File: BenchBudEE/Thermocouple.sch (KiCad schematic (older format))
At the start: 0 parts

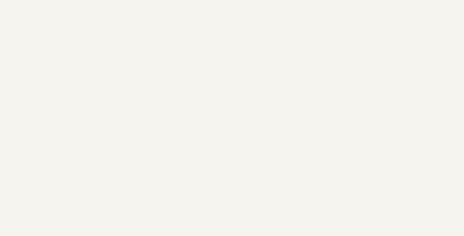
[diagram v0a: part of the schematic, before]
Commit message: Defined block inputs and outputs.
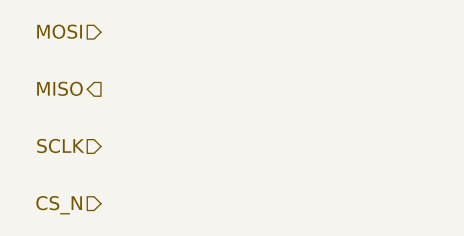
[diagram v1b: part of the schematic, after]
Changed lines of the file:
@@
 Text HLabel 5950 3150 2    60   Input ~ 0
 TC IN -
+Text HLabel 2300 2500 0    60   Input ~ 0
+MOSI
+Text HLabel 2300 2750 0    60   Output ~ 0
+MISO
+Text HLabel 2300 3000 0    60   Input ~ 0
+SCLK
+Text HLabel 2300 3250 0    60   Input ~ 0
+CS_N
 $EndSCHEMATC

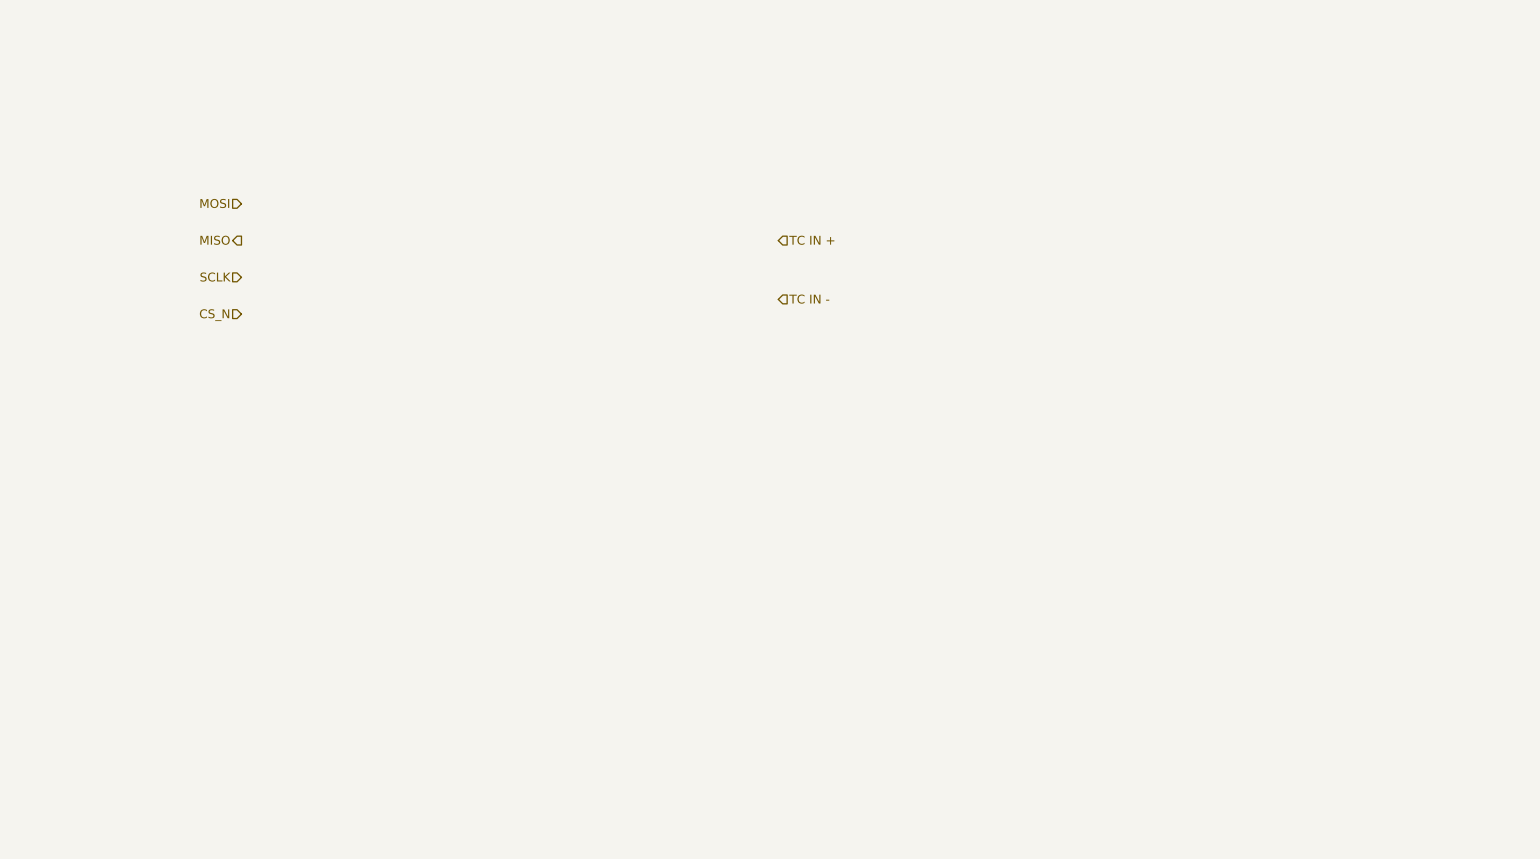
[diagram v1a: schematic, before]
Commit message: Fleshed out the thermocouple sheet, in block form.
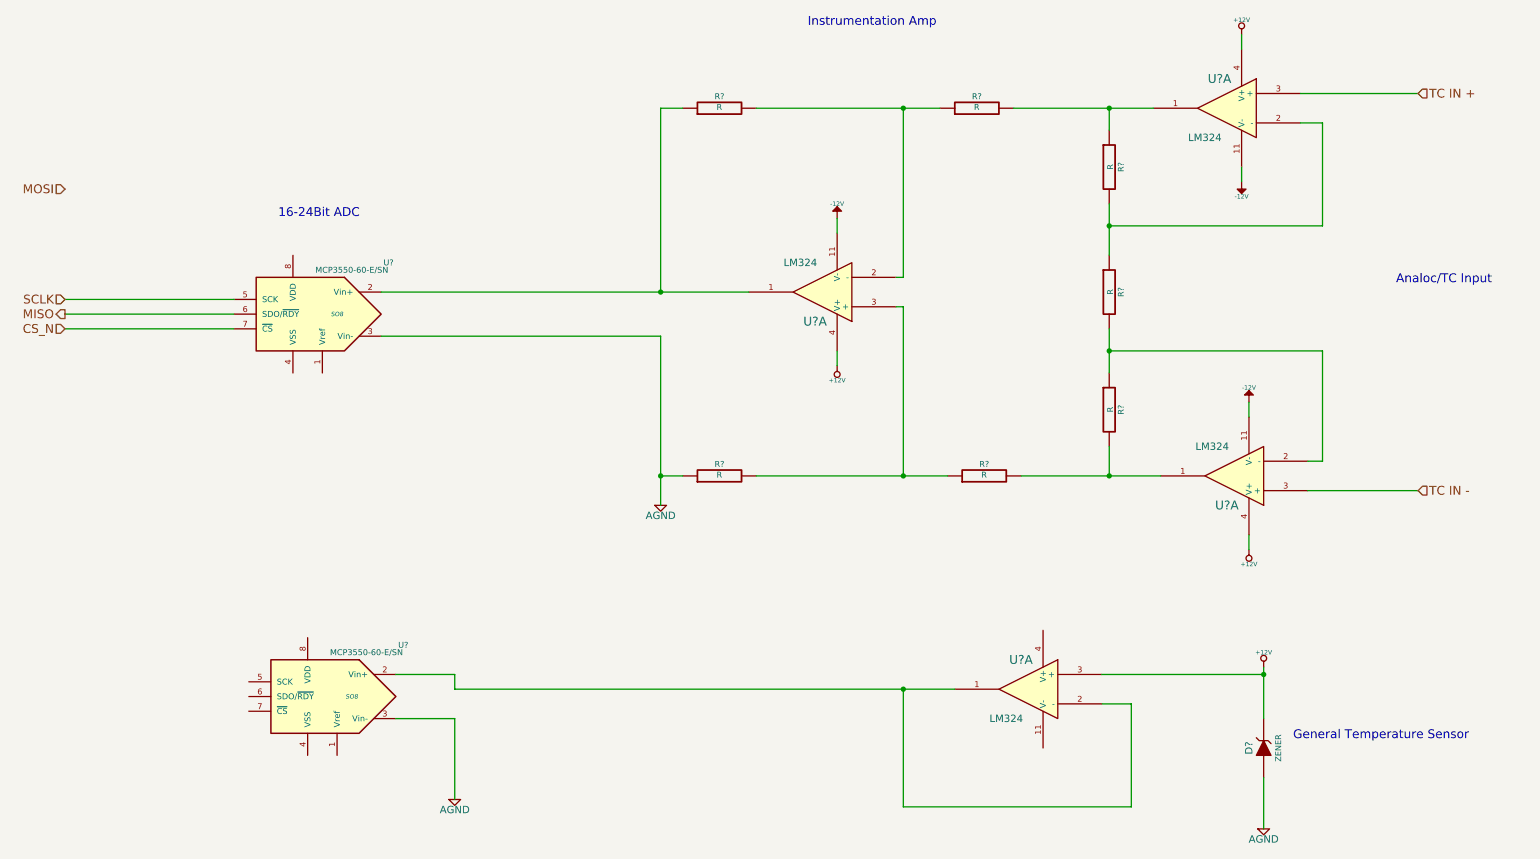
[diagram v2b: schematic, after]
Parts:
- added D?: ZENER, ~, symbol ZENER
- added R? (x7): R, ~, symbol R
- added U? (x4): LM324, symbol LM324
- added U? (x2): MCP3550-60-E/SN, SO8, symbol MCP3550-60-E/SN
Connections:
- net CS_N: now also U?.7 (~CS~)
- net MISO: now also U?.6 (SDO/~RDY~)
- net SCLK: now also U?.5 (SCK)
- net TC IN +: now also U?.3 (+)
- net TC IN -: now also U?.3 (+)
- new net: R?.1, R?.2, U?.1
- new net: R?.1, R?.2, U?.2 (-) (x3)
- new net: R?.2, R?.2, U?.1
- new net: R?.1, U?.1, U?.2 (Vin+)
- new net: R?.1, R?.2, U?.3 (+)
- new net: U?.1, U?.2 (-), U?.2 (Vin+)
- new net +12V: D?.2 (K), U?.3 (+), U?.4 (V+), U?.4 (V+), U?.4 (V+)
- new net -12V: U?.11 (V-), U?.11 (V-), U?.11 (V-)
- new net AGND: D?.1 (A), R?.1, U?.3 (Vin-), U?.3 (Vin-)
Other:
- note added: "16-24Bit ADC"
- note added: "Analoc/TC Input"
- note added: "General Temperature Sensor"
- note added: "Instrumentation Amp"
